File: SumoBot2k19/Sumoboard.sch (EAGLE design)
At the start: 24 parts

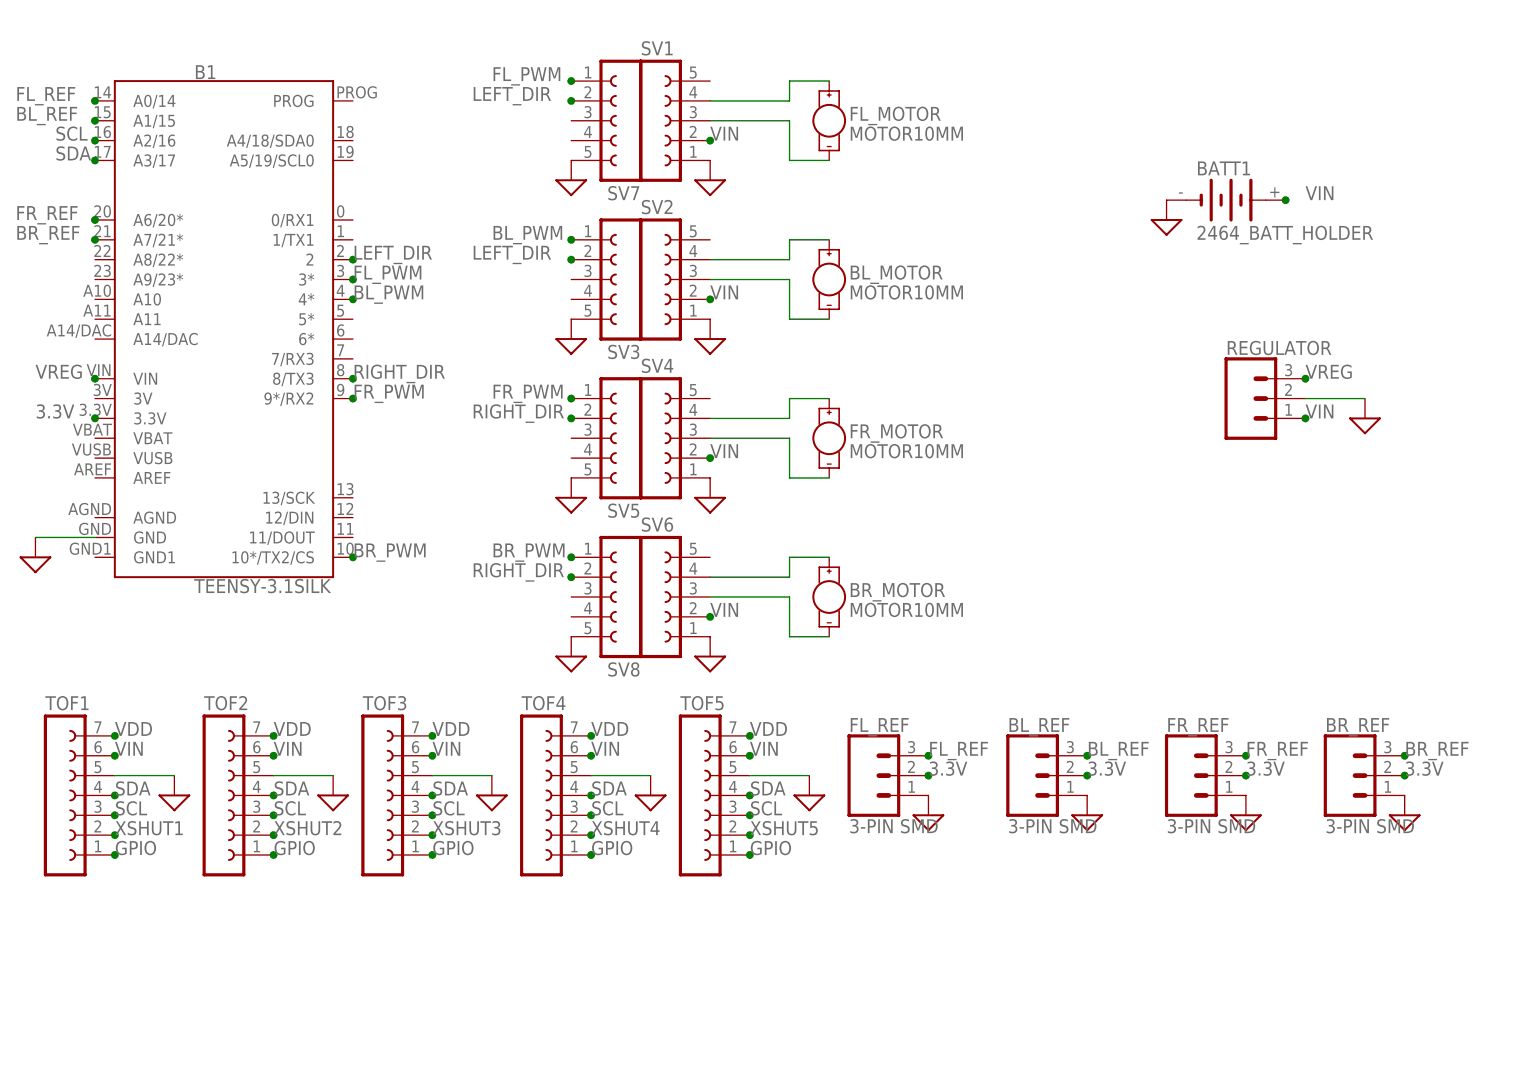
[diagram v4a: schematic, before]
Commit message: added bypass capacitors, added IR receiver
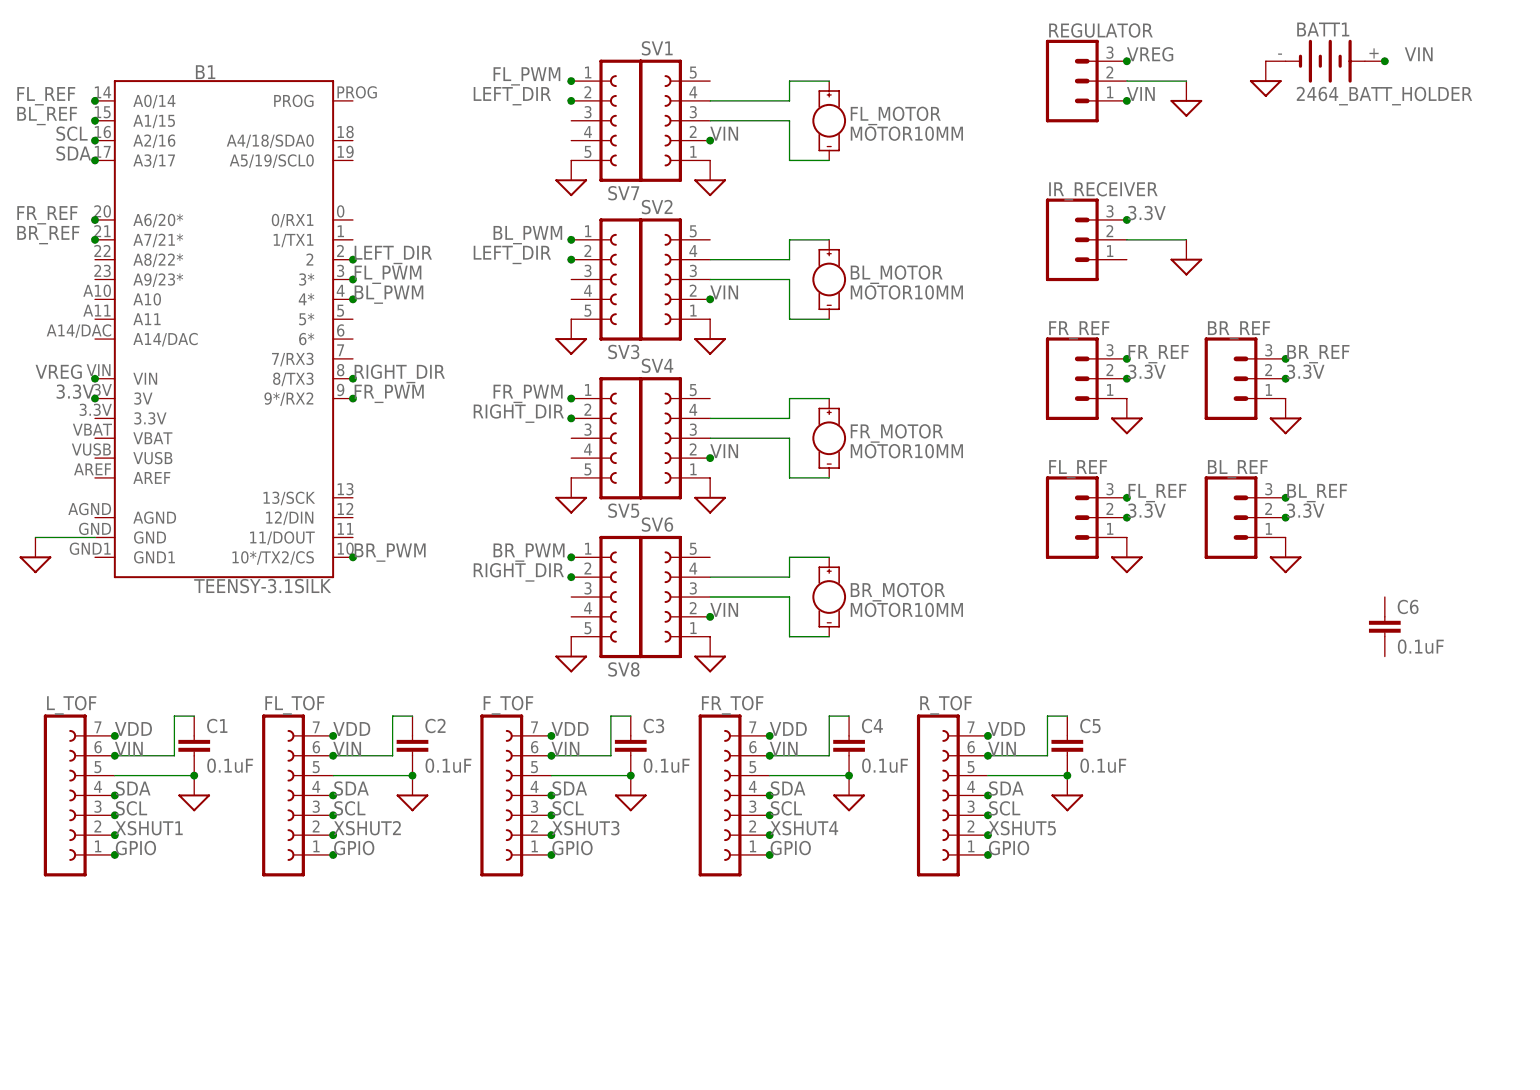
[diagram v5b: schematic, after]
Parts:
- removed TOF2, TOF3, TOF4, TOF5: (no value), con-lsta:FE07-1
- added C1, C2, C3, C4, C5, C6: 0.1uF, SparkFun-Capacitors:0.1UF-0603-25V-5%
- added FL_TOF, FR_TOF, F_TOF, R_TOF: (no value), con-lsta:FE07-1
- added IR_RECEIVER: (no value), SparkFun-Connectors:CONN_03
- renumbered TOF1 to L_TOF
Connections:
- net 3.3V: now also B1.3V, IR_RECEIVER.3; no longer B1.3.3V
- net GND: now also C1.2, C2.2, C3.2, C4.2, C5.2, FL_TOF.5, FR_TOF.5, F_TOF.5, IR_RECEIVER.2, R_TOF.5; no longer TOF2.5, TOF3.5, TOF4.5, TOF5.5
- net GPIO: now also FL_TOF.1, FR_TOF.1, F_TOF.1, R_TOF.1; no longer TOF2.1, TOF3.1, TOF4.1, TOF5.1
- net SCL: now also FL_TOF.3, FR_TOF.3, F_TOF.3, R_TOF.3; no longer TOF2.3, TOF3.3, TOF4.3, TOF5.3
- net SDA: now also FL_TOF.4, FR_TOF.4, F_TOF.4, R_TOF.4; no longer TOF2.4, TOF3.4, TOF4.4, TOF5.4
- net VDD: now also FL_TOF.7, FR_TOF.7, F_TOF.7, R_TOF.7; no longer TOF2.7, TOF3.7, TOF4.7, TOF5.7
- net VIN: now also C1.1, C2.1, C3.1, C4.1, C5.1, FL_TOF.6, FR_TOF.6, F_TOF.6, R_TOF.6; no longer TOF2.6, TOF3.6, TOF4.6, TOF5.6
- net XSHUT2: now also FL_TOF.2; no longer TOF2.2
- net XSHUT3: now also F_TOF.2; no longer TOF3.2
- net XSHUT4: now also FR_TOF.2; no longer TOF4.2
- net XSHUT5: now also R_TOF.2; no longer TOF5.2
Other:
- moved on the sheet: BATT1, BL_REF, BR_REF, FL_REF, FR_REF, REGULATOR

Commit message: added bypass caps to TOF sensors, motor drivers, and regulator
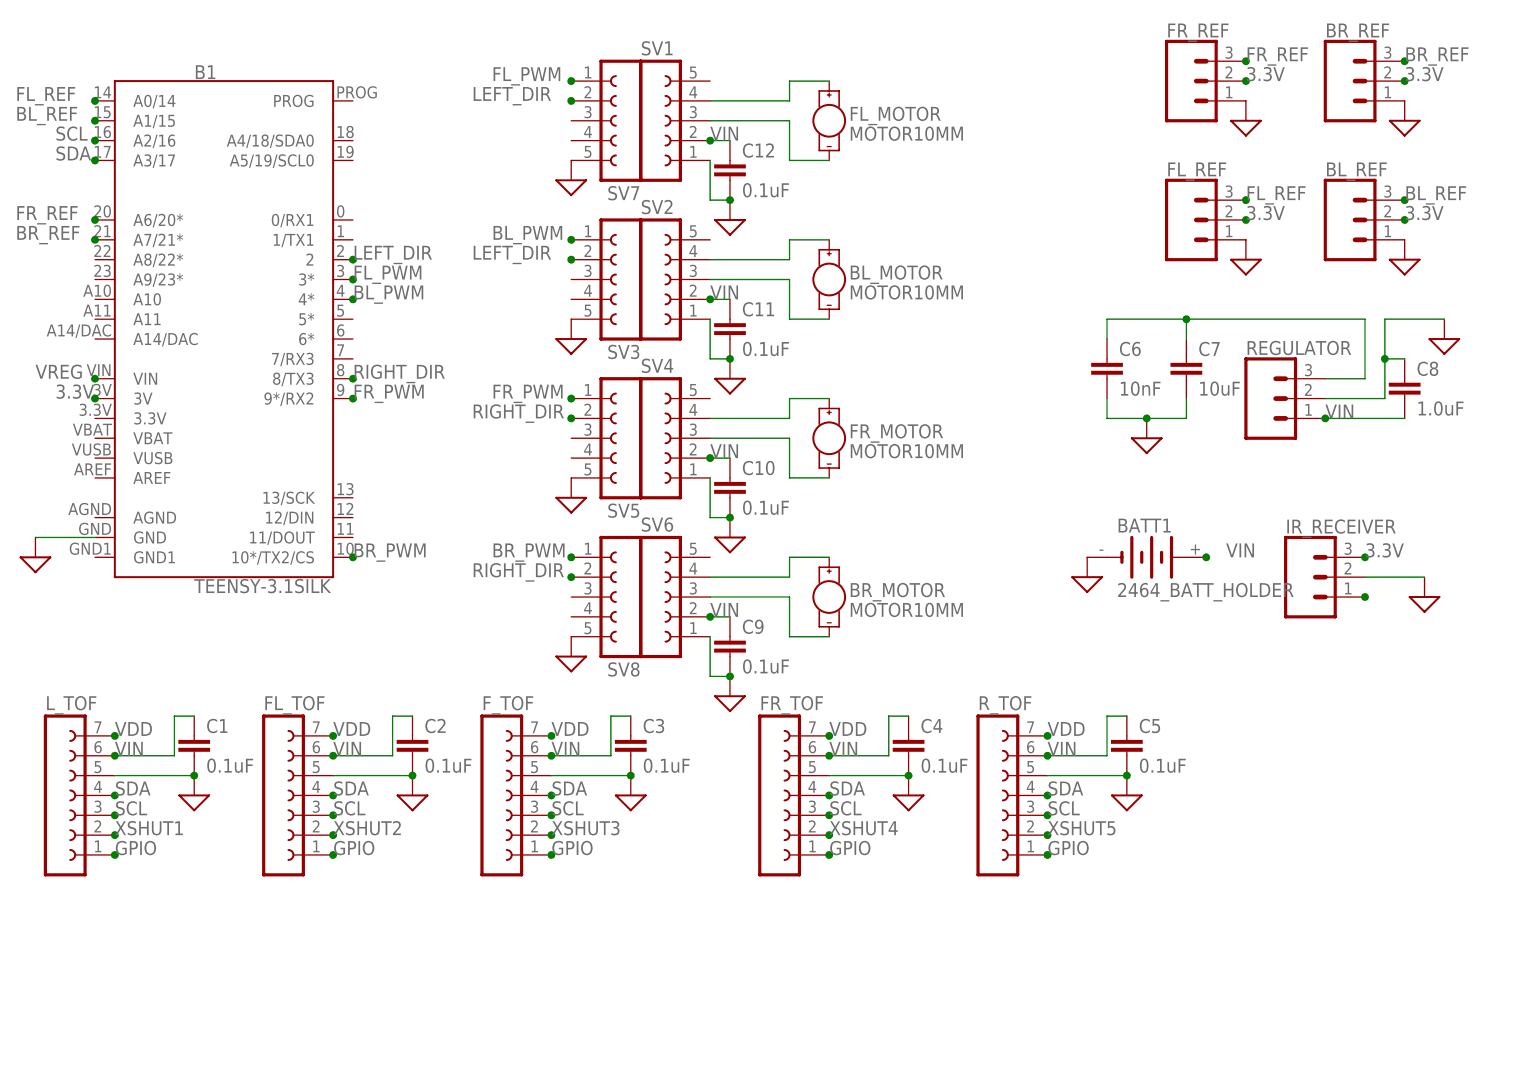
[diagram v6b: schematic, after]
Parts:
- added C10, C11, C12, C9: 0.1uF, SparkFun-Capacitors:0.1UF-0603-25V-5%
- added C7: 10uF, SparkFun-Capacitors:10UF-0603-6.3V-20%
- added C8: 1.0uF, SparkFun-Capacitors:1.0UF-0603-16V-10%
- C6: value 0.1uF -> 10nF; device SparkFun-Capacitors:0.1UF-0603-25V-5% -> SparkFun-Capacitors:10NF-0603-50V-10%
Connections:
- new net VIN1: C10.1
- new net VIN2: C11.1
- new net VIN3: C12.1
- new net VOUT: IR_RECEIVER.1
- net 3.3V: now also C6.1, C7.1, REGULATOR.3
- net GND: now also C10.2, C11.2, C12.2, C6.2, C7.2, C8.1, C9.2
- net VIN: now also C8.2, C9.1
- net VREG: no longer REGULATOR.3
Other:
- moved on the sheet: BATT1, BL_REF, BR_REF, C4, C5, C6, FL_REF, FR_REF, FR_TOF, IR_RECEIVER, REGULATOR, R_TOF

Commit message: Reverting back to the previous state of the project at f10550aeea0dc74b4494af4baa6c277cfe62f025
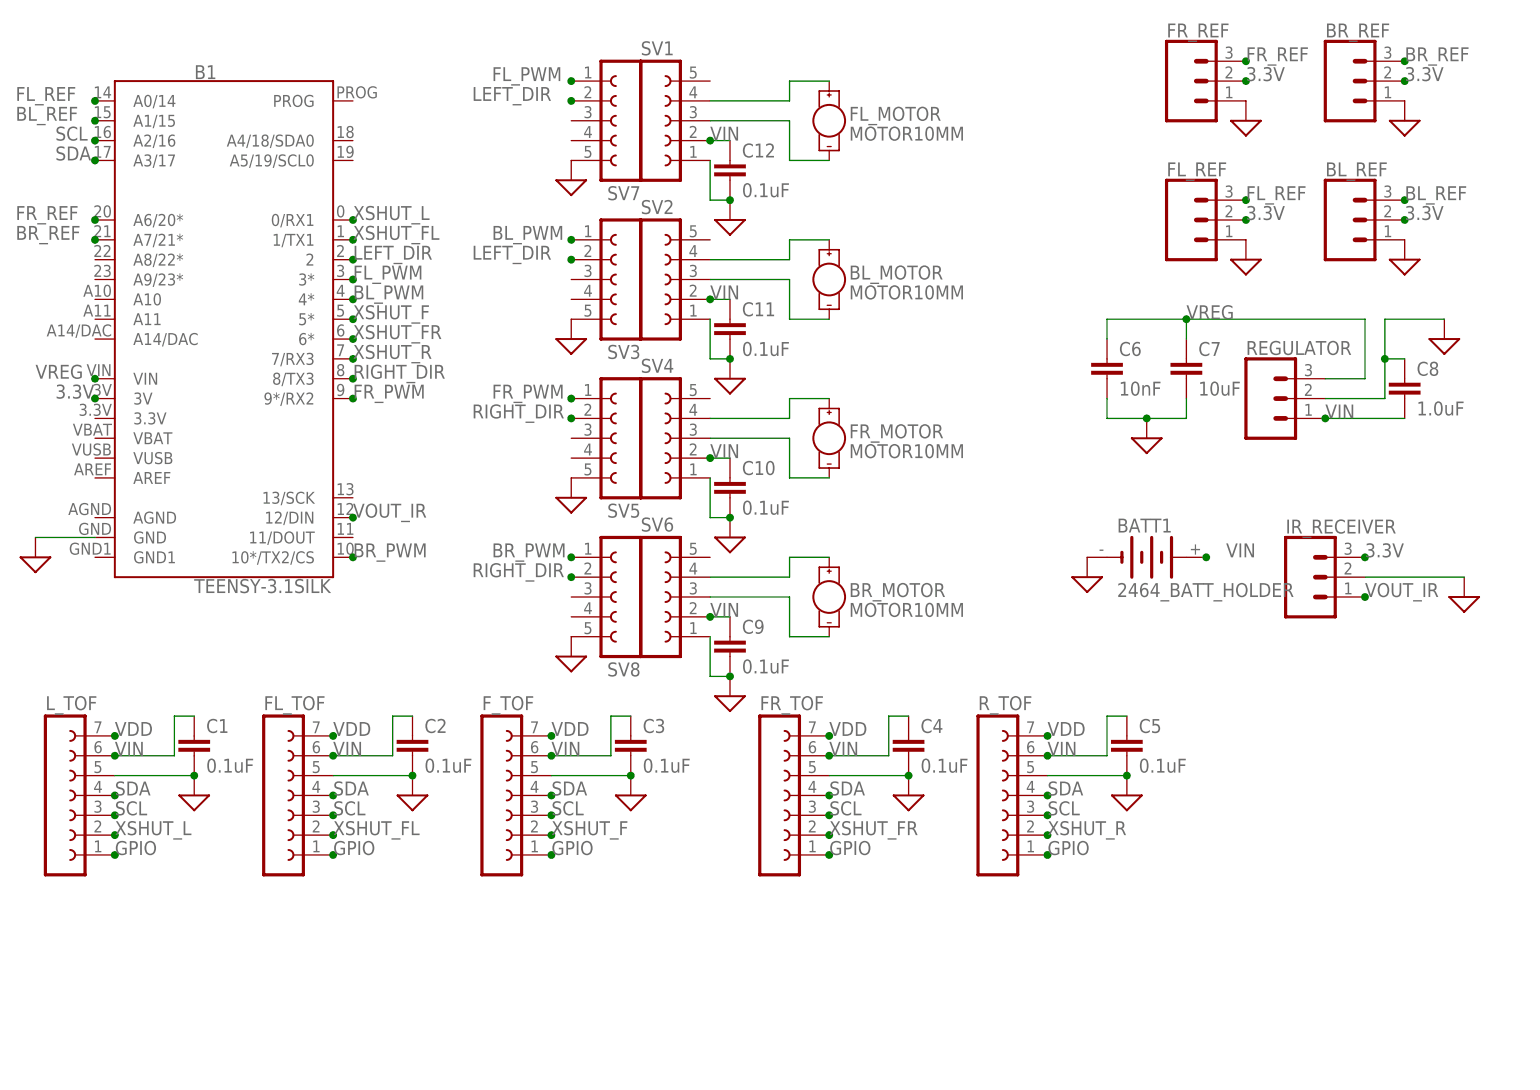
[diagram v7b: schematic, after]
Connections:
- removed net VOUT: IR_RECEIVER.1
- removed net XSHUT1: L_TOF.2
- removed net XSHUT2: FL_TOF.2
- removed net XSHUT3: F_TOF.2
- removed net XSHUT4: FR_TOF.2
- removed net XSHUT5: R_TOF.2
- new net VOUT_IR: B1.12/DIN, IR_RECEIVER.1
- new net XSHUT_F: B1.5*, F_TOF.2
- new net XSHUT_FL: B1.1/TX1, FL_TOF.2
- new net XSHUT_FR: B1.6*, FR_TOF.2
- new net XSHUT_L: B1.0/RX1, L_TOF.2
- new net XSHUT_R: B1.7/RX3, R_TOF.2
- net 3.3V: no longer C6.1, C7.1, REGULATOR.3
- net VREG: now also C6.1, C7.1, REGULATOR.3
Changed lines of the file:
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@@
 <attribute name="NAME" x="152.4" y="46.228" size="1.778" layer="95" font="vector"/>
 </instance>
-<instance part="GND21" gate="G$1" x="170.18" y="40.64" smashed="yes"/>
+<instance part="GND21" gate="G$1" x="175.26" y="40.64" smashed="yes"/>
 <instance part="C1" gate="G$1" x="12.7" y="17.78" smashed="yes">
 <attribute name="NAME" x="14.224" y="20.701" size="1.778" layer="95" font="vector"/>
@@
 <pinref part="IR_RECEIVER" gate="J$1" pin="2"/>
 <pinref part="GND21" gate="G$1" pin="GND"/>
-<wire x1="162.56" y1="40.64" x2="170.18" y2="40.64" width="0.1524" layer="91"/>
+<wire x1="162.56" y1="40.64" x2="175.26" y2="40.64" width="0.1524" layer="91"/>
 </segment>
 <segment>
@@
 </segment>
 </net>
-<net name="XSHUT1" class="0">
+<net name="XSHUT_L" class="0">
 <segment>
 <pinref part="L_TOF" gate="G$1" pin="2"/>
@@
 <label x="2.54" y="7.62" size="1.778" layer="95"/>
 </segment>
+<segment>
+<pinref part="B1" gate="G$1" pin="0/RX1"/>
+<junction x="33.02" y="86.36"/>
+<label x="33.02" y="86.36" size="1.778" layer="95"/>
+</segment>
 </net>
 <net name="GPIO" class="0">
@@
 <junction x="0" y="66.04"/>
 <label x="-7.62" y="66.04" size="1.778" layer="95"/>
-</segment>
-</net>
-<net name="3.3V" class="0">
-<segment>
-<pinref part="FL_REF" gate="J$1" pin="2"/>
-<junction x="147.32" y="86.36"/>
-<label x="147.32" y="86.36" size="1.778" layer="95"/>
-</segment>
-<segment>
-<pinref part="BL_REF" gate="J$1" pin="2"/>
-<junction x="167.64" y="86.36"/>
-<label x="167.64" y="86.36" size="1.778" layer="95"/>
-</segment>
-<segment>
-<pinref part="FR_REF" gate="J$1" pin="2"/>
-<junction x="147.32" y="104.14"/>
-<label x="147.32" y="104.14" size="1.778" layer="95"/>
-</segment>
-<segment>
-<pinref part="BR_REF" gate="J$1" pin="2"/>
-<junction x="167.64" y="104.14"/>
-<label x="167.64" y="104.14" size="1.778" layer="95"/>
-</segment>
-<segment>
-<pinref part="B1" gate="G$1" pin="3V"/>
-<junction x="0" y="63.5"/>
-<label x="-5.08" y="63.5" size="1.778" layer="95"/>
-</segment>
-<segment>
-<pinref part="IR_RECEIVER" gate="J$1" pin="3"/>
-<junction x="162.56" y="43.18"/>
-<label x="162.56" y="43.18" size="1.778" layer="95"/>
 </segment>
 <segment>
@@
 <junction x="139.7" y="73.66"/>
 <wire x1="162.56" y1="73.66" x2="162.56" y2="66.04" width="0.1524" layer="91"/>
+<label x="139.7" y="73.66" size="1.778" layer="95"/>
+</segment>
+</net>
+<net name="3.3V" class="0">
+<segment>
+<pinref part="FL_REF" gate="J$1" pin="2"/>
+<junction x="147.32" y="86.36"/>
+<label x="147.32" y="86.36" size="1.778" layer="95"/>
+</segment>
+<segment>
+<pinref part="BL_REF" gate="J$1" pin="2"/>
+<junction x="167.64" y="86.36"/>
+<label x="167.64" y="86.36" size="1.778" layer="95"/>
+</segment>
+<segment>
+<pinref part="FR_REF" gate="J$1" pin="2"/>
+<junction x="147.32" y="104.14"/>
+<label x="147.32" y="104.14" size="1.778" layer="95"/>
+</segment>
+<segment>
+<pinref part="BR_REF" gate="J$1" pin="2"/>
+<junction x="167.64" y="104.14"/>
+<label x="167.64" y="104.14" size="1.778" layer="95"/>
+</segment>
+<segment>
+<pinref part="B1" gate="G$1" pin="3V"/>
+<junction x="0" y="63.5"/>
+<label x="-5.08" y="63.5" size="1.778" layer="95"/>
+</segment>
+<segment>
+<pinref part="IR_RECEIVER" gate="J$1" pin="3"/>
+<junction x="162.56" y="43.18"/>
+<label x="162.56" y="43.18" size="1.778" layer="95"/>
 </segment>
 </net>
@@
 </segment>
 </net>
-<net name="XSHUT2" class="0">
+<net name="XSHUT_FL" class="0">
 <segment>
 <pinref part="FL_TOF" gate="G$1" pin="2"/>
@@
 <label x="30.48" y="7.62" size="1.778" layer="95"/>
 </segment>
-</net>
-<net name="XSHUT3" class="0">
+<segment>
+<pinref part="B1" gate="G$1" pin="1/TX1"/>
+<junction x="33.02" y="83.82"/>
+<label x="33.02" y="83.82" size="1.778" layer="95"/>
+</segment>
+</net>
+<net name="XSHUT_F" class="0">
 <segment>
 <pinref part="F_TOF" gate="G$1" pin="2"/>
@@
 <label x="58.42" y="7.62" size="1.778" layer="95"/>
 </segment>
-</net>
-<net name="XSHUT4" class="0">
+<segment>
+<pinref part="B1" gate="G$1" pin="5*"/>
+<junction x="33.02" y="73.66"/>
+<label x="33.02" y="73.66" size="1.778" layer="95"/>
+</segment>
+</net>
+<net name="XSHUT_FR" class="0">
 <segment>
 <pinref part="FR_TOF" gate="G$1" pin="2"/>
@@
 <label x="93.98" y="7.62" size="1.778" layer="95"/>
 </segment>
-</net>
-<net name="XSHUT5" class="0">
+<segment>
+<pinref part="B1" gate="G$1" pin="6*"/>
+<junction x="33.02" y="71.12"/>
+<label x="33.02" y="71.12" size="1.778" layer="95"/>
+</segment>
+</net>
+<net name="XSHUT_R" class="0">
 <segment>
 <pinref part="R_TOF" gate="G$1" pin="2"/>
@@
 <label x="121.92" y="7.62" size="1.778" layer="95"/>
 </segment>
+<segment>
+<pinref part="B1" gate="G$1" pin="7/RX3"/>
+<junction x="33.02" y="68.58"/>
+<label x="33.02" y="68.58" size="1.778" layer="95"/>
+</segment>
 </net>
 <net name="FL_REF" class="0">
@@
 </segment>
 </net>
-<net name="VOUT" class="0">
+<net name="VOUT_IR" class="0">
 <segment>
 <pinref part="IR_RECEIVER" gate="J$1" pin="1"/>
 <junction x="162.56" y="38.1"/>
-</segment>
-</net>
+<label x="162.56" y="38.1" size="1.778" layer="95"/>
+</segment>
+<segment>
+<pinref part="B1" gate="G$1" pin="12/DIN"/>
+<junction x="33.02" y="48.26"/>
+<label x="33.02" y="48.26" size="1.778" layer="95"/>
+</segment>
+</net>
